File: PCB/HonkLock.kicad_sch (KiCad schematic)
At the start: 8 parts, among them J1 Conn_01x03_Pin, J2 Conn_01x06_Pin, J3 Conn_01x04_Pin, U1 Waveshare_ESP32_S3_Zero

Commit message: Carrier board PCB
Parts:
- added SW1, SW2, SW3: SW_Push, Button_Switch_THT:SW_PUSH_6mm, symbol Switch:SW_Push
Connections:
- net GND: now also SW1.2, SW2.2, SW3.2
- net at U1.5 (GP2): now also SW1.1
- net at U1.6 (GP3): now also SW2.1
- net at U1.7 (GP4): now also SW3.1
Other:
- moved on the sheet: J2

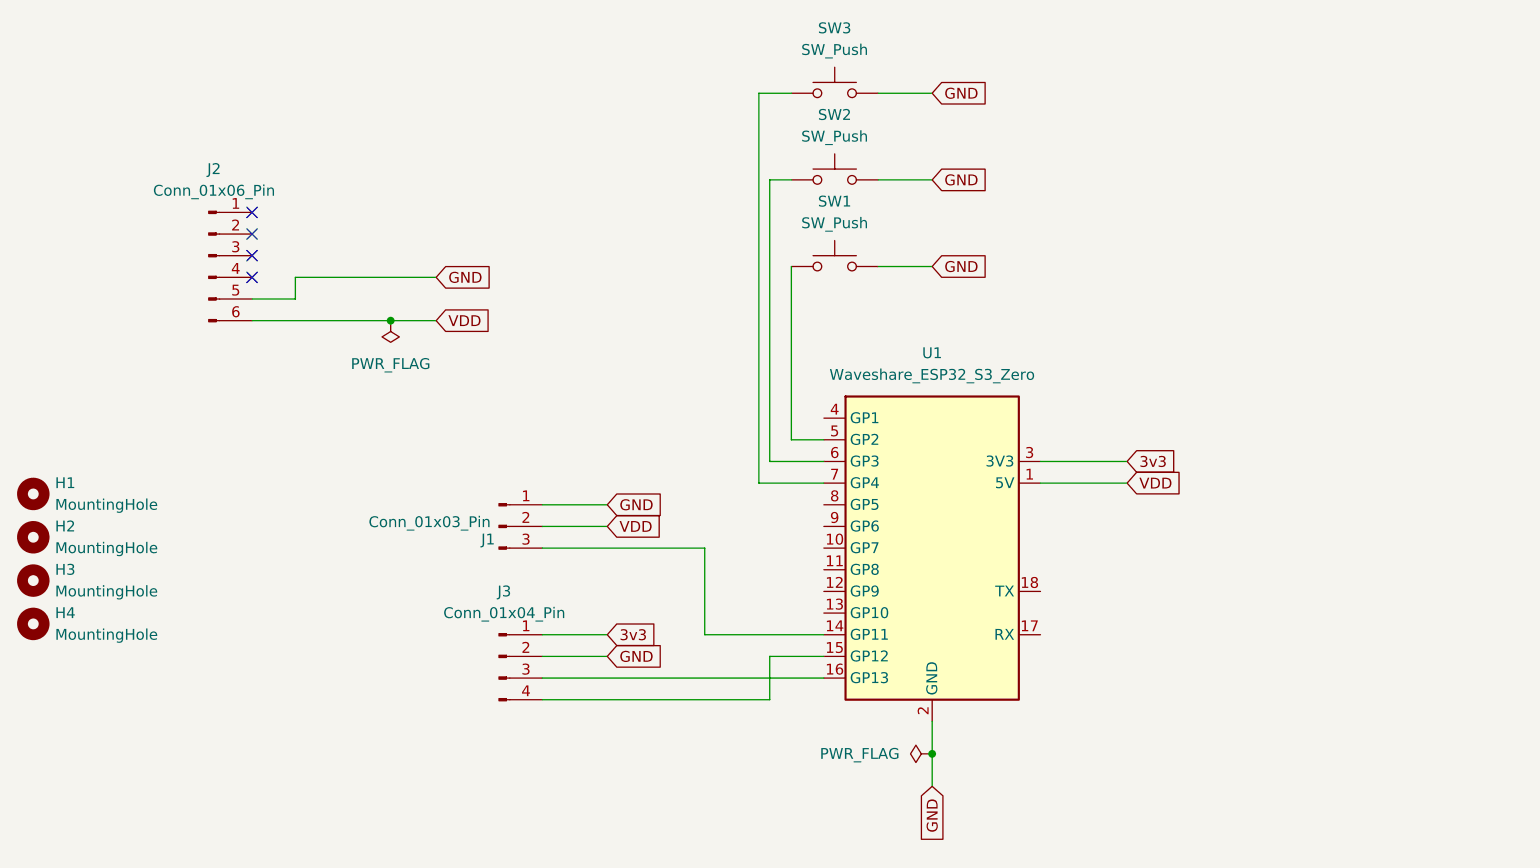
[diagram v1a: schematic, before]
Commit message: switched to the correct ESP32 dev board, added a capacitor, added a forth switch
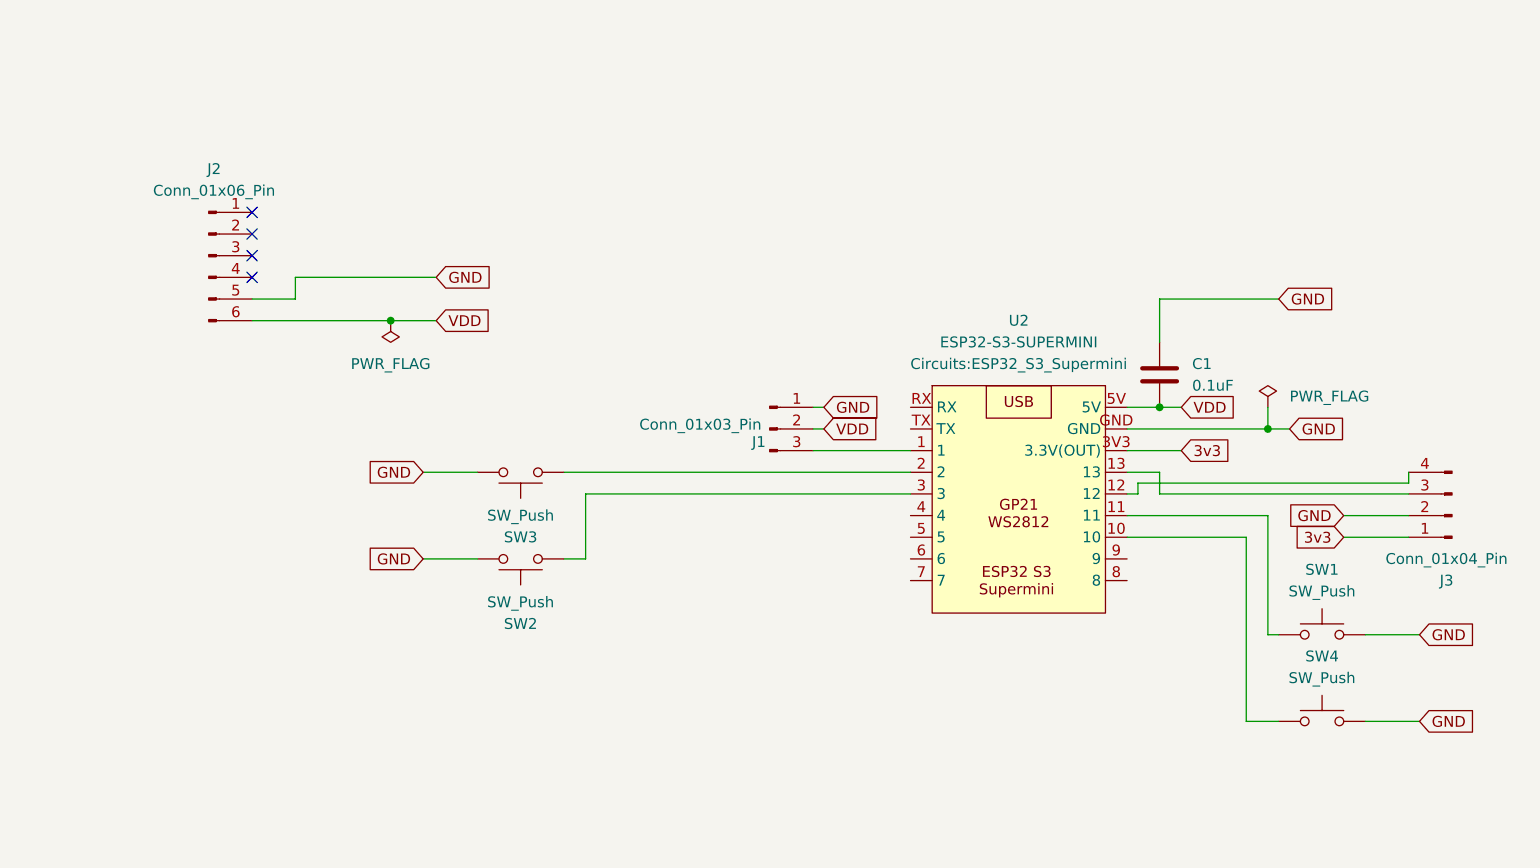
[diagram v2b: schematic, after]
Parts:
- removed H1, H2, H3, H4: MountingHole, MountingHole:MountingHole_2.7mm_M2.5_Pad, symbol Mechanical:MountingHole
- removed U1: Waveshare_ESP32_S3_Zero, Paul:Waveshare_ESP32_S3_Zero_Unspecified, symbol Paul:Waveshare_ESP32_S3_Zero
- added C1: 0.1uF, Capacitor_THT:C_Disc_D3.0mm_W1.6mm_P2.50mm, symbol Device:C
- added SW4: SW_Push, Button_Switch_THT:SW_PUSH_6mm, symbol Switch:SW_Push
- added U2: ESP32-S3-SUPERMINI, Circuits:ESP32_S3_Supermini, symbol ESP32S3SuperMini:ESP32-S3-Supermini
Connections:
- net 3v3: now also U2.3V3 (3.3V(OUT))
- net GND: now also C1.1, SW4.2, U2.GND
- net VDD: now also C1.2, U2.5V
- net at SW1.1: now also U2.11
- net at J1.3 (Pin_3): now also U2.1
- net at J3.4 (Pin_4): now also U2.12
- net at J3.3 (Pin_3): now also U2.13
- net at SW2.1: now also U2.3
- net at SW3.1: now also U2.2
- new net: SW4.1, U2.10
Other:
- moved on the sheet: J1, J3, SW1, SW2, SW3
